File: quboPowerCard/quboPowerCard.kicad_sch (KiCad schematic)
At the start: 15 parts, among them J4 Conn_01x04_Pin, J5 Conn_02x40_Odd_Even, Q1 IRF5305PbF, Q2 IRF5305PbF, U3 TSR2-2450, U4 TSR2-2433, U5 TSR2-2450

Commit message: Reverted broken name change
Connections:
- net NJSW1 renamed NPSW1
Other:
- note removed: "PiPower Converter"
- moved on the sheet: J5, U1

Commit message: pi card start
still needs resistors and capacitors put in, confirmation of pi 5v converter set up, and general clean up
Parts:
- removed R2: 10kO, Resistor_SMD:R_0805_2012Metric_Pad1.20x1.40mm_HandSolder, symbol PowerboardRev5-eagle-import:R-US_R0805
- removed U2: ~, Custom:72W_CONV, symbol Custom:EHHD006A0B
- removed U5: TSR2-2450, Custom:TSR2 DC/DC Converter, symbol PowerboardRev5-eagle-import:TSR2-2450
- added J6: 1720420202, customRAM:SUPERSABRE_2CIRCUIT, symbol supersabre:1720420202
- added PS1: THL_25-2411WI, customRAM:CONV_THL_25-2411WI, symbol customRAM:THL_25-2411WI
- J4: footprint Fuse:1.25__FUSECLIPS -> customRAM:1.25__FUSECLIPS
- J5: footprint Samtec Custom:Samtec_HLE-140-02-L-DV-PE_2x40_P2.54mm_Horizontal -> customRAM:SAMTEC_HLE-140-02-L-DV-PE
- U1: footprint Custom:240W_CONV -> customRAM:240W_CONV
- U3: footprint Custom:TSR2 DC/DC Converter -> customRAM:CONV_TSR_2-2450
- U4: footprint Custom:TSR2 DC/DC Converter -> customRAM:CONV_TSR2-2433
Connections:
- net +24V: now also J6.1
- net GND: now also J6.2, PS1.2 (-VIN(GND))
- net PiPower5V: now also PS1.3 (+VOUT)
- net VBATT renamed V_POWER
- net V_POWER: now also PS1.1 (+VIN(VCC))
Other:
- note added: "24V Connector"
- note added: "Convert to 5V for Pi"
- moved on the sheet: C1

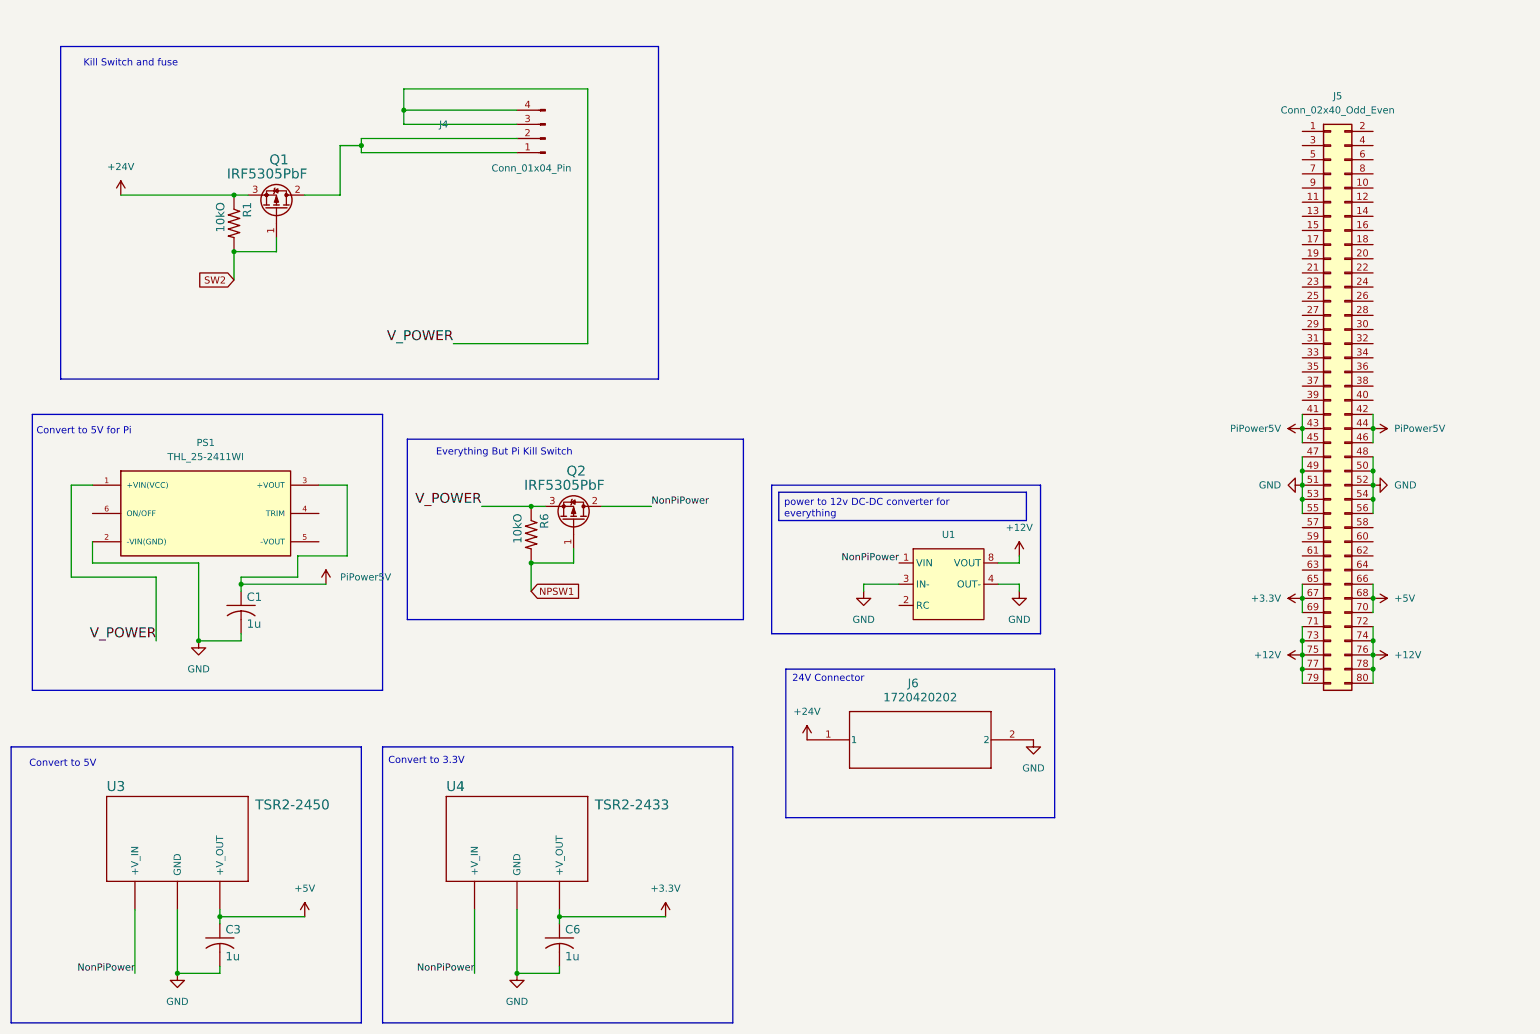
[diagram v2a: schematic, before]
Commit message: power card update
put the resistors/capacitors in and added in the traces, also added the two switch jsts.
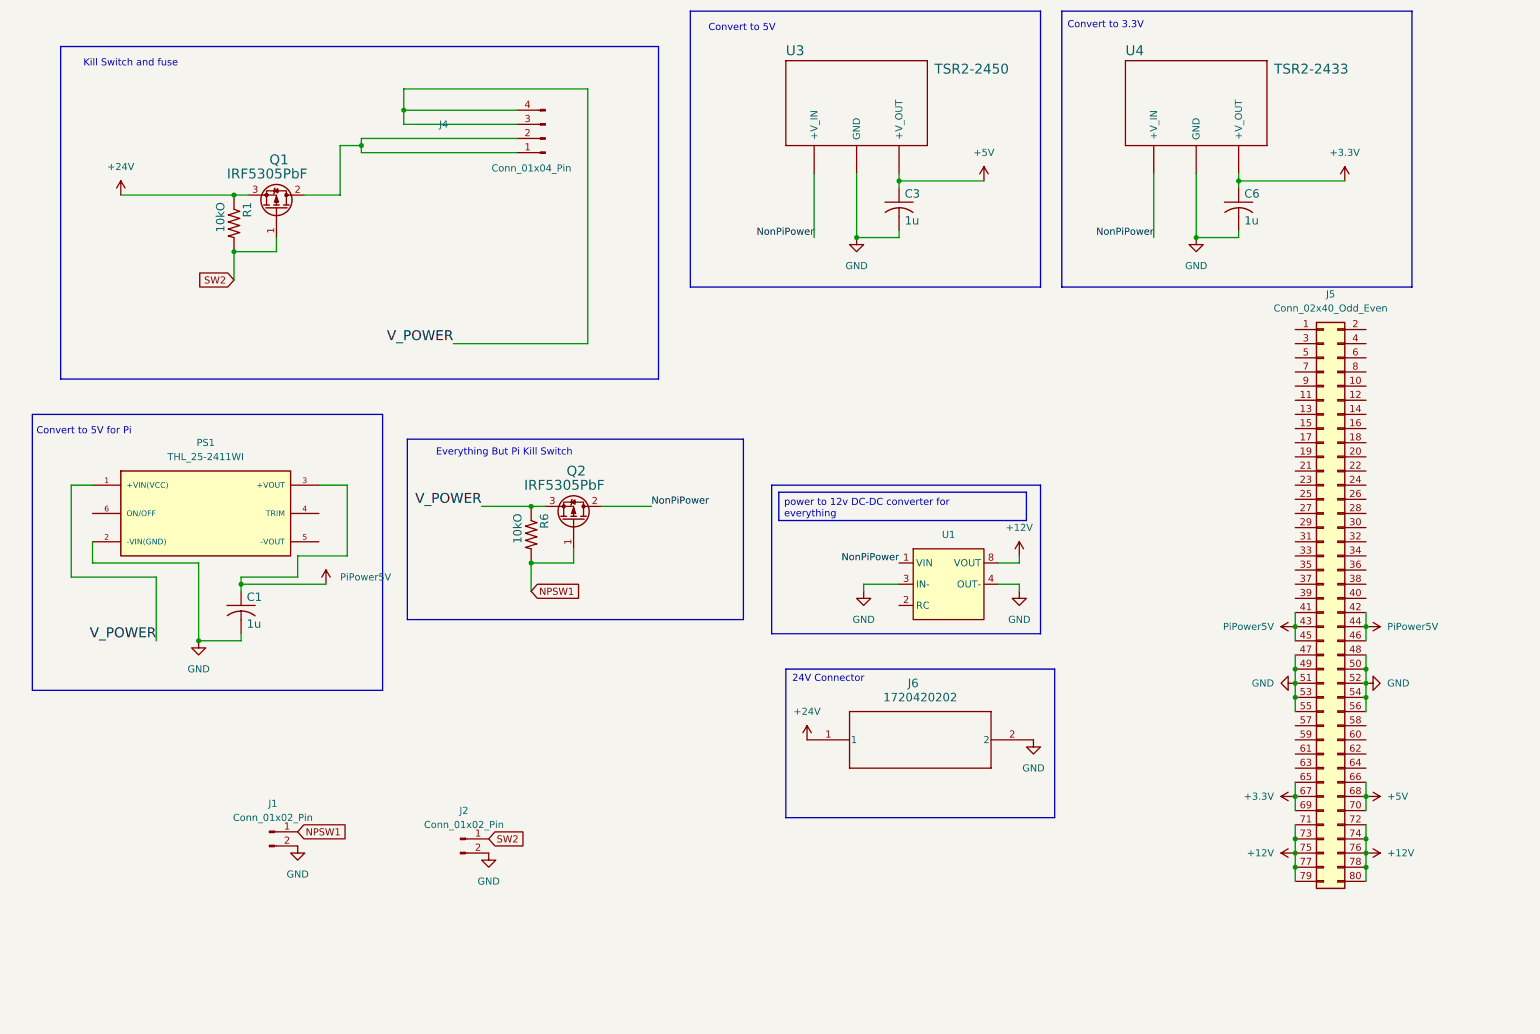
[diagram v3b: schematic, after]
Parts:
- added J1, J2: Conn_01x02_Pin, customRAM:JST_PH_B2B-PH-K_1x02_P2.00mm_Vertical, symbol Connector:Conn_01x02_Pin
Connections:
- net GND: now also J1.2 (Pin_2), J2.2 (Pin_2)
- net NPSW1: now also J1.1 (Pin_1)
- net SW2: now also J2.1 (Pin_1)
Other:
- moved on the sheet: C3, C6, J5, U3, U4

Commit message: Added Silkscreen, 12V Drops, Holes
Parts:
- added H1, H2, H3: MountingHole, MountingHole:MountingHole_2.2mm_M2, symbol Mechanical:MountingHole
- added J10, J3, J7, J8, J9: Conn_01x02_Pin, Connector_JST:JST_PH_B2B-PH-K_1x02_P2.00mm_Vertical, symbol Connector:Conn_01x02_Pin
- J1, J2: footprint customRAM:JST_PH_B2B-PH-K_1x02_P2.00mm_Vertical -> Connector_JST:JST_PH_B2B-PH-K_1x02_P2.00mm_Vertical
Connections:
- net +12V: now also J10.1 (Pin_1), J3.1 (Pin_1), J7.1 (Pin_1), J8.1 (Pin_1), J9.1 (Pin_1)
- net GND: now also J10.2 (Pin_2), J3.2 (Pin_2), J7.2 (Pin_2), J8.2 (Pin_2), J9.2 (Pin_2)
